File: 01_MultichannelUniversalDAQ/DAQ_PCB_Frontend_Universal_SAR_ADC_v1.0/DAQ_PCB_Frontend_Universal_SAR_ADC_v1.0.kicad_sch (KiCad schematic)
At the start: 6 parts

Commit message: bugfix
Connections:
- net GND: now reaches H3.1
- net GND: now also H1.1, H2.1, H4.1, H5.1, H6.1
- no-connect marks 7 -> 1

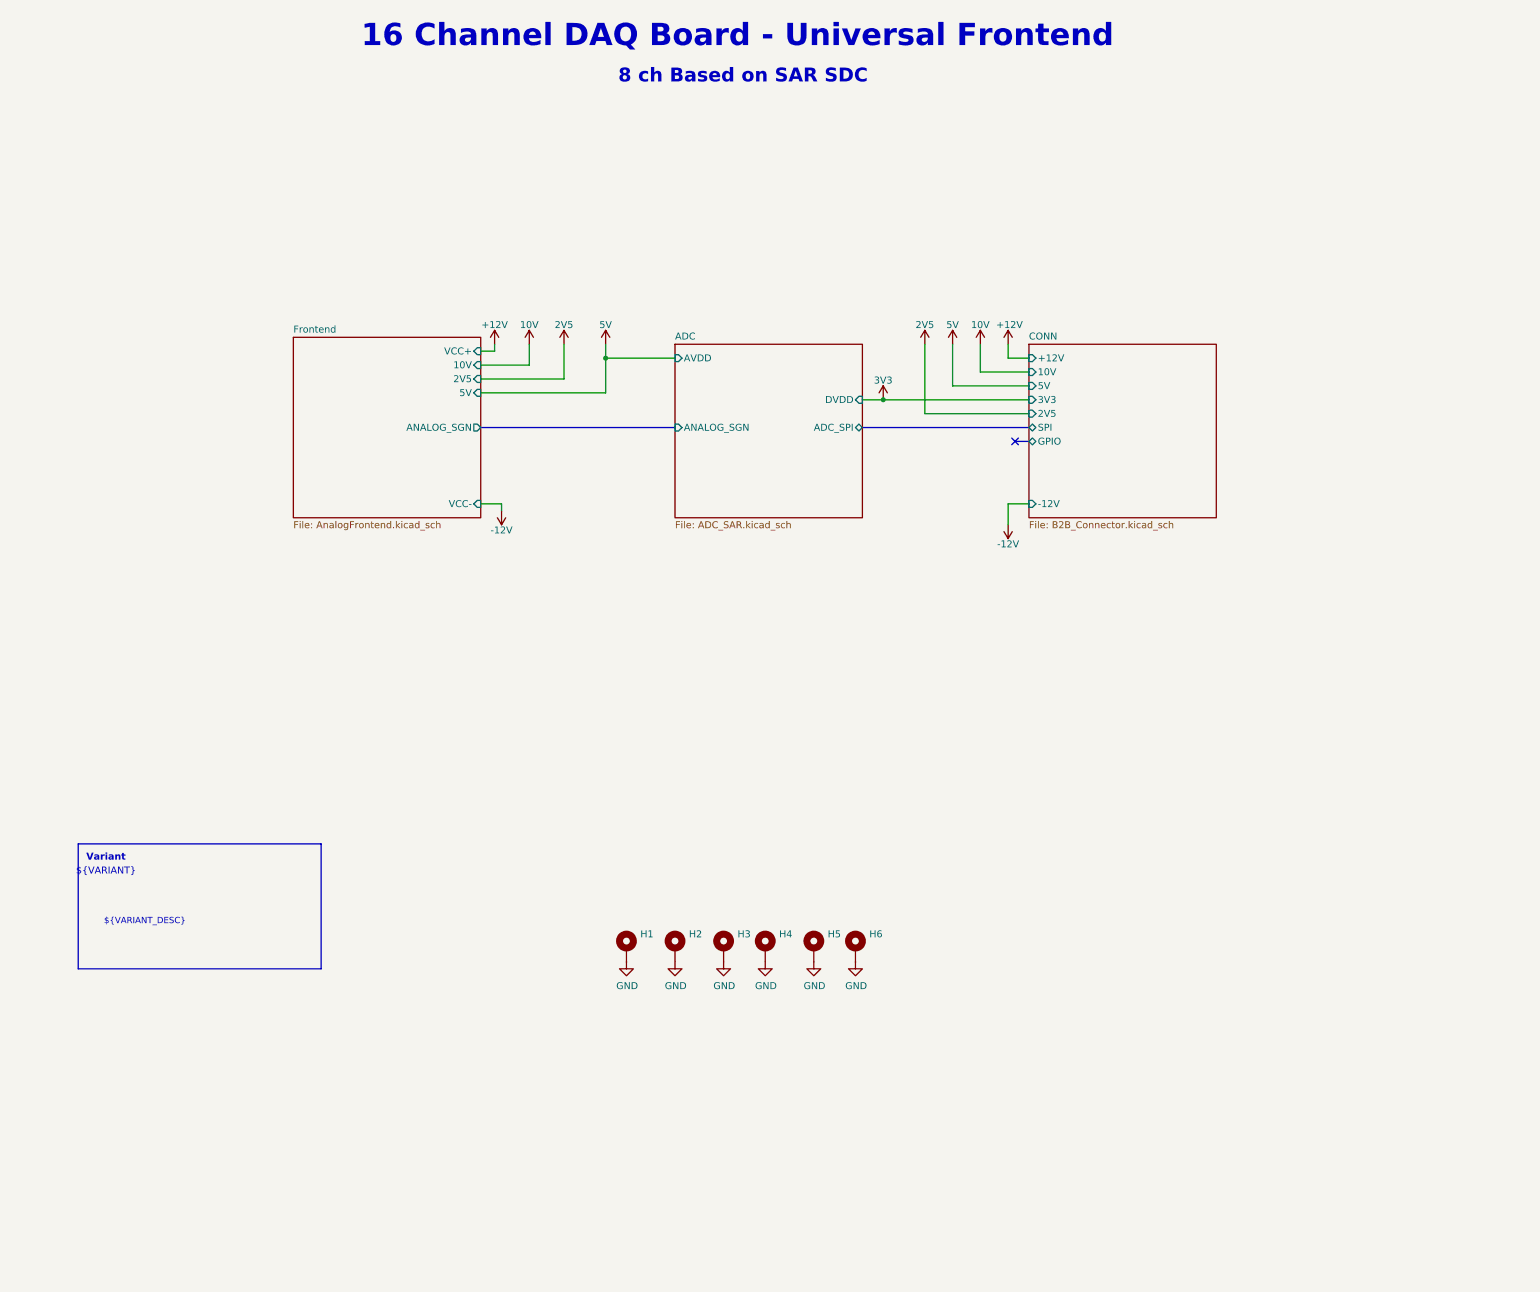
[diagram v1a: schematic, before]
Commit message: ADC és preamp in progress
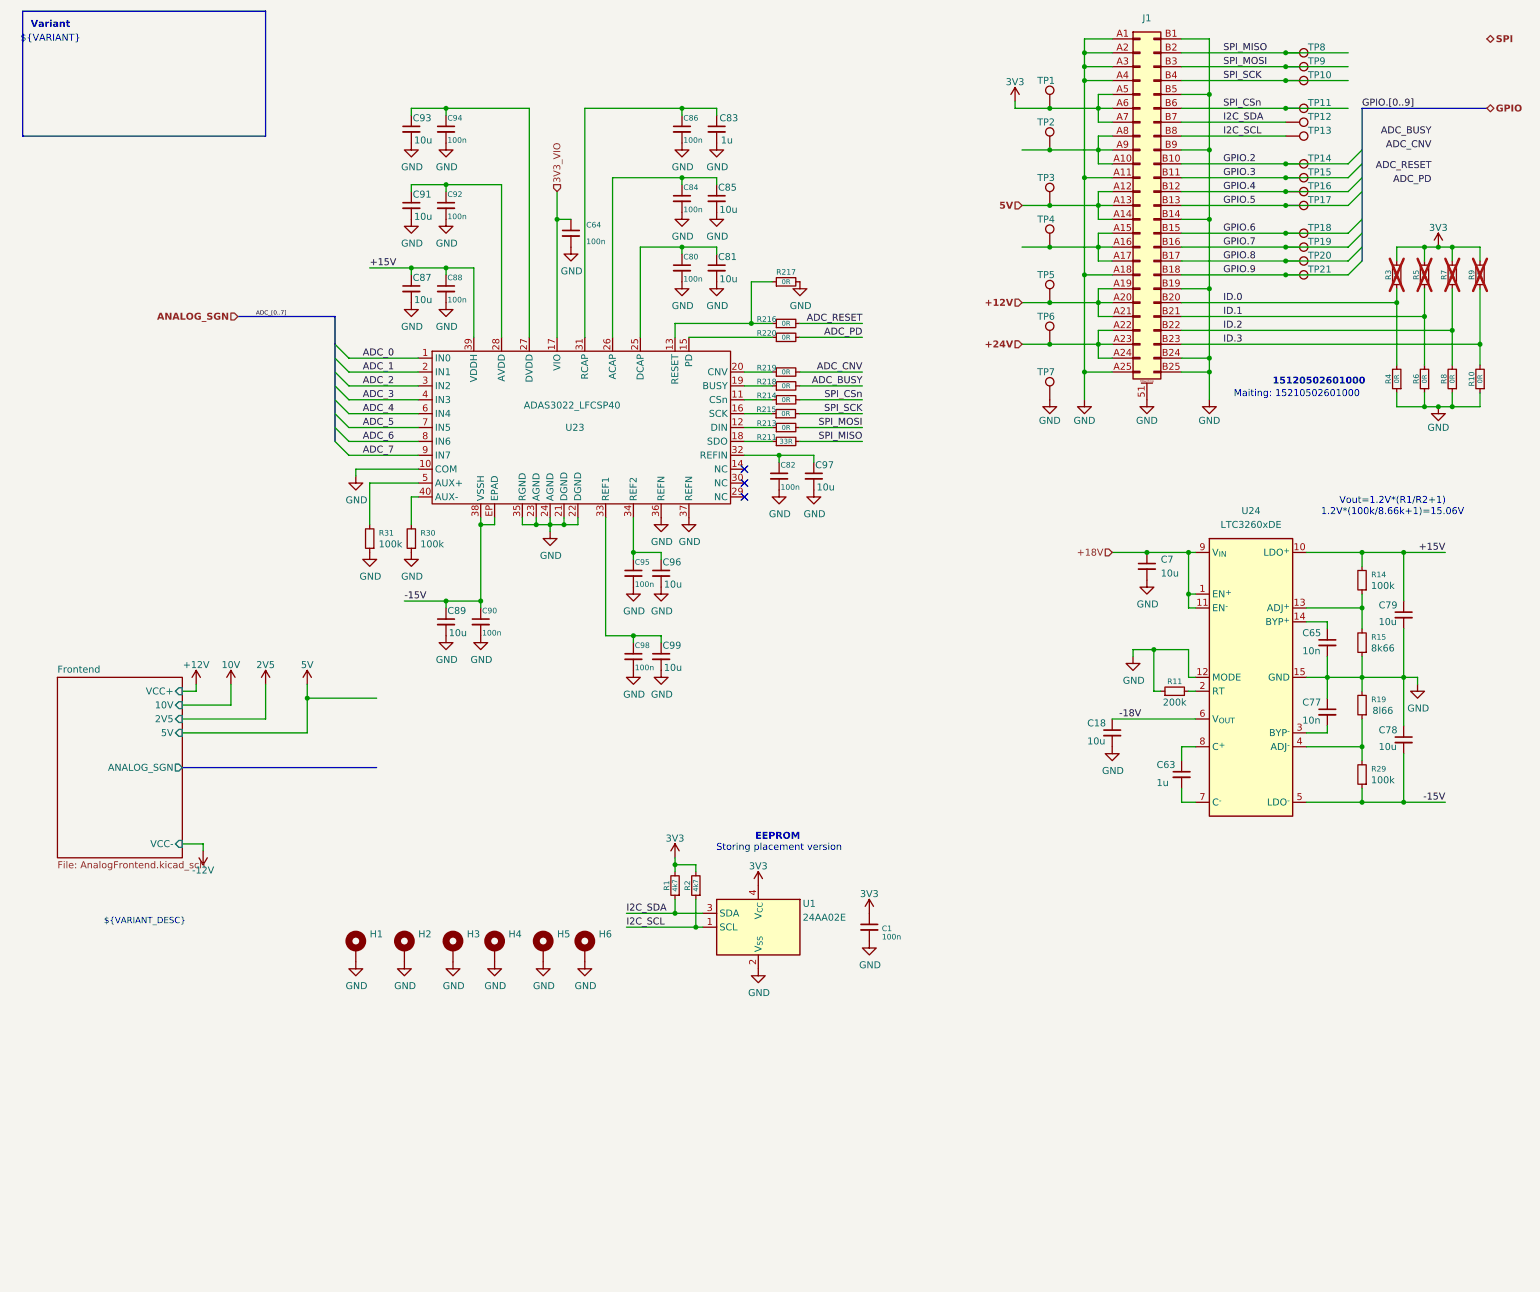
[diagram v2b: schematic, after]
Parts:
- added C1, C64, C80, C82, C84, C86, C88, C90, C92, C94, C95, C98: 100n, Capacitor_SMD:C_0603_1608Metric_Pad1.08x0.95mm_HandSolder, symbol Device:C_Small
- added C18, C7, C78, C79, C81, C85, C87, C89, C91, C93, C96, C97, C99: 10u, symbol Device:C_Small
- added C63, C83: 1u, symbol Device:C_Small
- added C65, C77: 10n, symbol Device:C_Small
- added J1: (no value), KJ_KiCadLib_Others_Footprint:15120502601000, symbol KJ_KiCadLib:CONN_02x25_Hartning_B2B
- added R1, R2: 4k7, Resistor_SMD:R_0603_1608Metric_Pad0.98x0.95mm_HandSolder, symbol Device:R_Small
- added R10, R213, R214, R215, R216, R217, R218, R219, R220, R3, R4, R5, R6, R7, R8, R9: 0R, Resistor_SMD:R_0603_1608Metric_Pad0.98x0.95mm_HandSolder, symbol Device:R_Small
- added R11: 200k, symbol Device:R_Small
- added R14, R29, R30, R31: 100k, symbol Device:R_Small
- added R15: 8k66, symbol Device:R_Small
- added R19: 8l66, symbol Device:R_Small
- added R211: 33R, Resistor_SMD:R_0603_1608Metric_Pad0.98x0.95mm_HandSolder, symbol Device:R_Small
- added TP1, TP10, TP11, TP12, TP13, TP14, TP15, TP16, TP17, TP18, TP19, TP2, TP20, TP21, TP3, TP4, TP5, TP6, TP7, TP8, TP9: TestPoint, TestPoint:TestPoint_Pad_D1.0mm, symbol Connector:TestPoint
- added U1: 24AA02E, Package_TO_SOT_SMD:SOT-23-5, symbol Memory_EEPROM:24AA02E-OT
- added U23: ADAS3022_LFCSP40, symbol MeMeKicadLib:ADAS3022_LFCSP40
- added U24: LTC3260xDE, Package_DFN_QFN:DFN-14-1EP_3x4mm_P0.5mm_EP1.7x3.3mm, symbol Regulator_SwitchedCapacitor:LTC3260xDE
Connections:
- net +12V: now also J1.A19 (Pin_19a), J1.A20 (Pin_20a), J1.A21 (Pin_21a), TP5.1
- net 3V3: now also C1.1, J1.A5 (Pin_5a), J1.A6 (Pin_6a), J1.A7 (Pin_7a), R1.2, R2.2, R3.2, R5.2, R7.2, R9.2, TP1.1, U1.4 (V_{CC})
- net 5V: now also J1.A12 (Pin_12a), J1.A13 (Pin_13a), J1.A14 (Pin_14a), TP3.1
- net GND: now also C1.2, C18.2, C64.2, C65.2, C7.2, C77.1, C78.1, C79.2, C80.2, C81.2, C82.2, C83.2, C84.2, C85.2, C86.2, C87.2, C88.2, C89.2, C90.2, C91.2, C92.2, C93.2, C94.2, C95.2, C96.2, C97.2, C98.2, C99.2, J1.51 (MountPin), J1.52 (MountPin), J1.53 (MountPin), J1.54 (MountPin), J1.A1 (Pin_1a), J1.A11 (Pin_11a), J1.A18 (Pin_18a), J1.A2 (Pin_2a), J1.A25 (Pin_25a), J1.A3 (Pin_3a), J1.A4 (Pin_4a), J1.B1 (Pin_1b), J1.B14 (Pin_14b), J1.B19 (Pin_19b), J1.B24 (Pin_24b), J1.B25 (Pin_25b), J1.B5 (Pin_5b), J1.B9 (Pin_9b), R10.1, R11.1, R15.1, R19.2, R217.2, R30.1, R31.1, R4.1, R6.1, R8.1, TP7.1, U1.2 (V_{SS}), U23.10 (COM), U23.21 (DGND), U23.22 (DGND), U23.23 (AGND), U23.24 (AGND), U23.35 (RGND), U23.36 (REFN), U23.37 (REFN), U24.12 (MODE), U24.15 (GND)
- new net: R219.1, U23.20 (CNV)
- new net: R218.1, U23.19 (BUSY)
- new net: R11.2, U24.2 (RT)
- new net: C93.1, C94.1, U23.27 (DVDD)
- new net: J1.A10 (Pin_10a), J1.A8 (Pin_8a), J1.A9 (Pin_9a), TP2.1
- new net: J1.A15 (Pin_15a), J1.A16 (Pin_16a), J1.A17 (Pin_17a), TP4.1
- new net: C82.1, C97.1, U23.32 (REFIN)
- new net: C91.1, C92.1, U23.28 (AVDD)
- new net: C80.1, C81.1, U23.25 (DCAP)
- new net: R14.1, R15.2, U24.13 (ADJ^{+})
- new net: C65.1, U24.14 (BYP^{+})
- new net: C98.1, C99.1, U23.33 (REF1)
- new net: R19.1, R29.2, U24.4 (ADJ^{-})
- new net: C83.1, C86.1, U23.31 (RCAP)
- new net: R215.1, U23.16 (SCK)
- new net: C63.1, U24.8 (C^{+})
- new net: C63.2, U24.7 (C^{-})
- new net: R31.2, U23.5 (AUX+)
- new net: R214.1, U23.11 (CSn)
- new net: C95.1, C96.1, U23.34 (REF2)
- new net: R216.1, R217.1, U23.13 (RESET)
- new net: R213.1, U23.12 (DIN)
- new net: R220.1, U23.15 (PD)
- new net: R211.1, U23.18 (SDO)
- new net: C84.1, C85.1, U23.26 (ACAP)
- new net: R30.2, U23.40 (AUX-)
- new net: C77.2, U24.3 (BYP^{-})
- new net +15V: C79.1, C87.1, C88.1, R14.2, U23.39 (VDDH), U24.10 (LDO^{+})
- new net +18V: C7.1, U24.1 (EN^{+}), U24.11 (EN^{-}), U24.9 (V_{IN})
- new net +24V: J1.A22 (Pin_22a), J1.A23 (Pin_23a), J1.A24 (Pin_24a), TP6.1
- new net -15V: C78.2, C89.1, C90.1, R29.1, U23.38 (VSSH), U23.EP (EPAD), U24.5 (LDO^{-})
- new net -18V: C18.1, U24.6 (V_{OUT})
- new net 3V3_VIO: C64.1, U23.17 (VIO)
- new net ADC_0: U23.1 (IN0)
- new net ADC_1: U23.2 (IN1)
- new net ADC_2: U23.3 (IN2)
- new net ADC_3: U23.4 (IN3)
- new net ADC_4: U23.6 (IN4)
- new net ADC_5: U23.7 (IN5)
- new net ADC_6: U23.8 (IN6)
- new net ADC_7: U23.9 (IN7)
- new net ADC_BUSY: R218.2
- new net ADC_CNV: R219.2
- new net ADC_PD: R220.2
- new net ADC_RESET: R216.2
- new net GPIO.2: J1.B10 (Pin_10b), TP14.1
- new net GPIO.3: J1.B11 (Pin_11b), TP15.1
- new net GPIO.4: J1.B12 (Pin_12b), TP16.1
- new net GPIO.5: J1.B13 (Pin_13b), TP17.1
- new net GPIO.6: J1.B15 (Pin_15b), TP18.1
- new net GPIO.7: J1.B16 (Pin_16b), TP19.1
- new net GPIO.8: J1.B17 (Pin_17b), TP20.1
- new net GPIO.9: J1.B18 (Pin_18b), TP21.1
- new net I2C_SCL: J1.B8 (Pin_8b), R2.1, TP13.1, U1.1 (SCL)
- new net I2C_SDA: J1.B7 (Pin_7b), R1.1, TP12.1, U1.3 (SDA)
- new net ID.0: J1.B20 (Pin_20b), R3.1, R4.2
- new net ID.1: J1.B21 (Pin_21b), R5.1, R6.2
- new net ID.2: J1.B22 (Pin_22b), R7.1, R8.2
- new net ID.3: J1.B23 (Pin_23b), R10.2, R9.1
- new net SPI_CSn: J1.B6 (Pin_6b), R214.2, TP11.1
- new net SPI_MISO: J1.B2 (Pin_2b), R211.2, TP8.1
- new net SPI_MOSI: J1.B3 (Pin_3b), R213.2, TP9.1
- new net SPI_SCK: J1.B4 (Pin_4b), R215.2, TP10.1
- no-connect marks 1 -> 3
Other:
- removed sheet ADC
- removed sheet CONN
- note added: "15120502601000"
- note added: "EEPROM"
- note added: "Maiting: 15210502601000"
- note added: "Storing placement version"
- note added: "Vout=1.2V*(R1/R2+1) 1.2V*(100k/8.66k+1)=15.06V"
- note removed: "16 Channel DAQ Board - Universal Frontend"
- note removed: "8 ch Based on SAR SDC"
- moved on the sheet: H1, H2, H3, H4, H5, H6

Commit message: ...
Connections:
- net 3V3_VIO is gone; now on net +3V3: C64.1, U23.17 (VIO)
- net 5V is gone; now on net +12V: J1.A12 (Pin_12a), J1.A13 (Pin_13a), J1.A14 (Pin_14a), TP3.1
- net GPIO.2 is gone; now on net ADC_BUSY: J1.B10 (Pin_10b), TP14.1
- net GPIO.3 is gone; now on net ADC_CNV: J1.B11 (Pin_11b), TP15.1
- net GPIO.4 is gone; now on net ADC_RESET: J1.B12 (Pin_12b), TP16.1
- net GPIO.5 is gone; now on net ADC_PD: J1.B13 (Pin_13b), TP17.1
- net +12V: no longer J1.A19 (Pin_19a), J1.A20 (Pin_20a), J1.A21 (Pin_21a), TP5.1
- net +18V: now also J1.A19 (Pin_19a), J1.A20 (Pin_20a), J1.A21 (Pin_21a), TP5.1
- net +24V: now also J1.A15 (Pin_15a), J1.A16 (Pin_16a), J1.A17 (Pin_17a), TP4.1; no longer J1.A22 (Pin_22a), J1.A23 (Pin_23a), J1.A24 (Pin_24a), TP6.1
- net +5V: now reaches J1.A10 (Pin_10a), J1.A8 (Pin_8a), J1.A9 (Pin_9a), TP2.1
- net 3V3 renamed +3V3
- net ADC_0 renamed CH1
- net ADC_1 renamed CH2
- net ADC_2 renamed CH3
- net ADC_3 renamed CH4
- net ADC_4 renamed CH5
- net ADC_5 renamed CH6
- net ADC_6 renamed CH7
- net ADC_7 renamed CH8
- net GPIO.6: no longer names the net of J1.B15 (Pin_15b), TP18.1
- net GPIO.7: no longer names the net of J1.B16 (Pin_16b), TP19.1
- net GPIO.8: no longer names the net of J1.B17 (Pin_17b), TP20.1
- net GPIO.9: no longer names the net of J1.B18 (Pin_18b), TP21.1
- new net: J1.A22 (Pin_22a), J1.A23 (Pin_23a), J1.A24 (Pin_24a), TP6.1
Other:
- removed sheet Frontend
- added sheet PREAMP1 (PreAmp.kicad_sch)
- added sheet PREAMP2 (PreAmp.kicad_sch)
- added sheet PREAMP3 (PreAmp.kicad_sch)
- added sheet PREAMP4 (PreAmp.kicad_sch)
- added sheet PREAMP5 (PreAmp.kicad_sch)
- added sheet PREAMP6 (PreAmp.kicad_sch)
- added sheet PREAMP7 (PreAmp.kicad_sch)
- added sheet PREAMP8 (PreAmp.kicad_sch)
- moved on the sheet: C1, H1, H2, H3, H4, H5, H6, J1, TP1, TP10, TP11, TP12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

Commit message: RefBuffer
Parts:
- added C78: 1u, symbol Device:C_Small
- added C79: 100n, Capacitor_SMD:C_0603_1608Metric_Pad1.08x0.95mm_HandSolder, symbol Device:C_Small
- added R179, R181: 100k, symbol Device:R_Small
- added R180: 10k, symbol Device:R_Small
- added R190, R191: 0R, Resistor_SMD:R_0603_1608Metric_Pad0.98x0.95mm_HandSolder, symbol Device:R_Small
- added R192, R193: (no value), symbol MeMeKicadLib:AORN1002AT5
- added U20: AD8397, symbol Device:Opamp_Dual
- renumbered C93 to C1, C80 to C10, C81 to C11, C87 to C12, C88 to C13, C82 to C14, C97 to C15, C7 to C16, C95 to C17, C96 to C18, C79 to C19, C94 to C2, C89 to C20, C90 to C21, C65 to C22, C98 to C23, C99 to C24, C77 to C25, C18 to C26, C78 to C27, C63 to C28, C1 to C29, C86 to C3, C83 to C4, C84 to C5, C85 to C6, C91 to C7, C92 to C8, C64 to C9, R3 to R1, R6 to R10, R8 to R11, R10 to R12, R218 to R13, R214 to R14, R215 to R15, R213 to R16, R211 to R17, R31 to R18, R30 to R19, R5 to R2, R14 to R20, R15 to R21, R11 to R22, R19 to R23, R29 to R24, R1 to R25, R2 to R26, R7 to R3, R9 to R4, R217 to R5, R216 to R6, R220 to R7, R219 to R8, R4 to R9, TP8 to TP1, TP15 to TP10, TP16 to TP11, TP3 to TP12, TP17 to TP13, TP18 to TP14, TP4 to TP15, TP19 to TP16, TP20 to TP17, TP21 to TP18, TP5 to TP19, TP9 to TP2, TP6 to TP20, TP7 to TP21, TP10 to TP3, TP1 to TP4, TP11 to TP5, TP12 to TP6, TP13 to TP7, TP2 to TP8, TP14 to TP9, U23 to U1, U24 to U2, U1 to U3
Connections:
- net +12V: now also R191.1
- net +5V: now also R190.1
- net GND: now also C78.2, C79.2, R192.1, R193.1, U20.4 (V-)
- net REF4.096: now reaches C14.1, C15.1, U1.32 (REFIN)
- net REF4.096: now also R180.2
- new net: R179.2, R193.7, R193.8, U20.2 (-)
- new net: C79.1, R180.1, U20.3 (+), U20.5 (+)
- new net: R181.2, R192.7, R192.8, U20.6 (-)
- new net: C78.1, R190.2, R191.2, U20.8 (V+)
- new net: R193.2, R193.3, R193.4
- new net: R192.2, R192.3, R192.4
- new net V4.096_A: R179.1, R193.5, R193.6, U20.1
- new net V4.096_B: R181.1, R192.5, R192.6, U20.7
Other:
- sheet PREAMP1 ports: added 4.096V; removed none
- sheet PREAMP2 ports: added 4.096V; removed none
- sheet PREAMP3 ports: added 4.096V; removed none
- sheet PREAMP4 ports: added 4.096V; removed none
- sheet PREAMP5 ports: added 4.096V; removed none
- sheet PREAMP6 ports: added 4.096V; removed none
- sheet PREAMP7 ports: added 4.096V; removed none
- sheet PREAMP8 ports: added 4.096V; removed none
- moved on the sheet: C1, C10, C11, C12, C13, C14, C15, C17, C18, C2, C20, C21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
